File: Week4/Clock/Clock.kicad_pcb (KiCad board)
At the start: 2 copper layers, 140 x 90 mm, 48 parts, among them J1 Power_inlet_vertical, J2 Conn_01x06, SW1 RotaryEncoder_Switch, SW2 Omron_B3F_SPST, U2 ATmega328-PU, U3 L7805_TO92, U4 DS1307_DIP-8, U5 MAX7219, U6 MAX7219, Y1 Crystal 16MHZ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

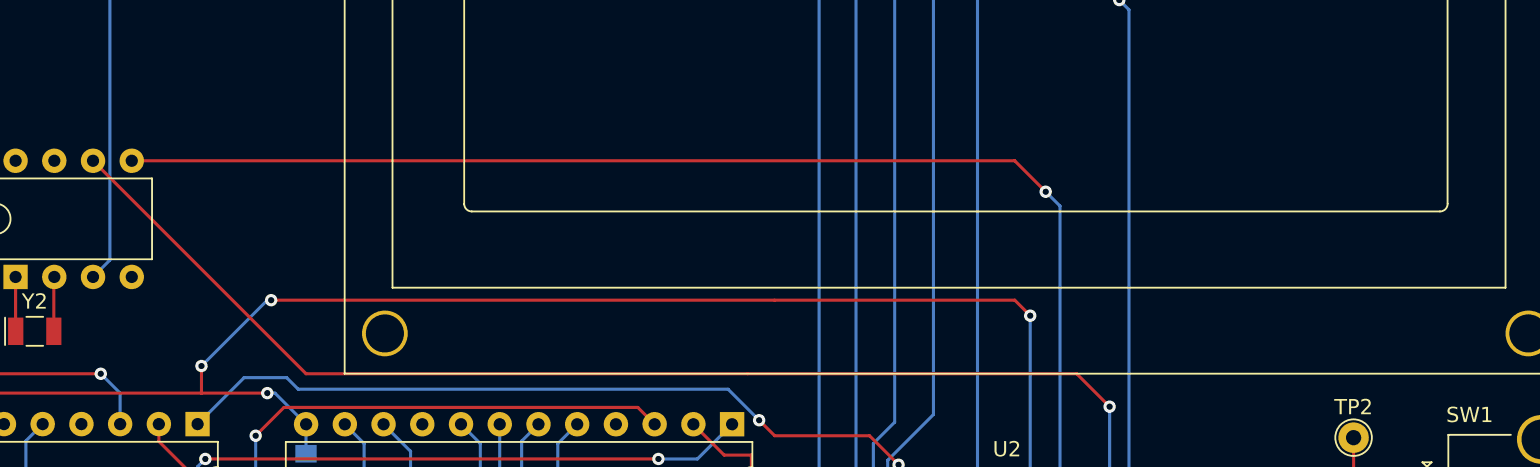
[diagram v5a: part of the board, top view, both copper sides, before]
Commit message: Week 6 Update* (Arduino Code)
Added additional Display modes now including Decimal and Binary mode found at https://bryang229.github.io/8x8Demo/ :) now we have 3 different ways to read time !
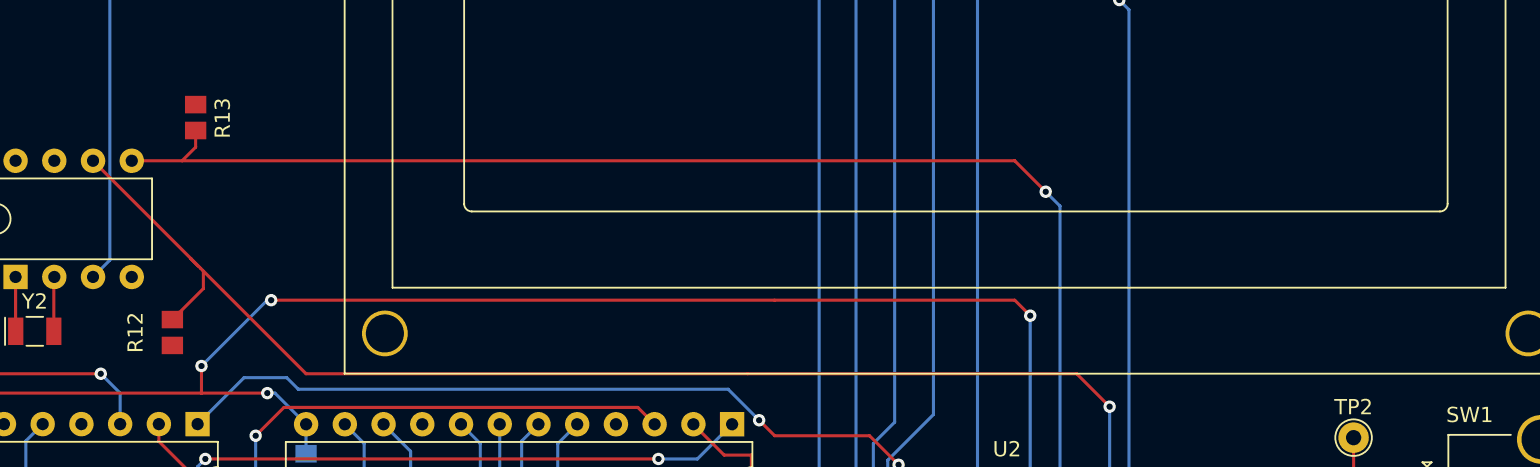
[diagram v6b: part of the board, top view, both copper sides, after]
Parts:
- added R12: R_0805_2.2K, footprints:R_0805_2012Metric, F.Cu at (118.7, 91.8)
- added R13: R_0805_2.2K, footprints:R_0805_2012Metric, F.Cu at (120.3, 77.7)
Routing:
- net A5 SCK: track 80.3 -> 85.1 mm
- net A4 SDA: track 84.0 -> 86.3 mm
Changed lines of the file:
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@@
     )
   )
+  (footprint "footprints:R_0805_2012Metric" (layer "F.Cu")
+    (at 118.745 91.782 90)
+    (descr "Resistor SMD 0805 (2012 Metric), square (rectangular) end terminal, IPC_7351 nominal, (Body size source: http://www.tortai-tech.com/upload/download/2011102023233369053.pdf), generated with kicad-footprint-generator")
+    (tags "resistor")
+    (property "Digikey PN" "311-2.20KCRCT-ND")
+    (property "MFG" "N/A")
+    (property "MPN" "N/A")
+    (property "Mouser PN" "N/A")
+    (property "Power" "N/A")
+    (property "Sheetfile" "Clock.kicad_sch")
+    (property "Sheetname" "")
+    (property "Tolerance" "N/A")
+    (attr smd)
+    (fp_text reference "R12" (at 0 -2.413 90) (layer "F.SilkS")
+      (effects (font (size 1 1) (thickness 0.15)))
+    )
+    (fp_text value "R_0805_2.2K" (at 0 1.65 90) (layer "F.Fab")
+      (effects (font (size 1 1) (thickness 0.15)))
+    )
+    (fp_text user "${REFERENCE}" (at 0 0 90) (layer "F.Fab")
+      (effects (font (size 0.5 0.5) (thickness 0.08)))
+    )
+    (fp_line (start -1.68 -0.95) (end 1.68 -0.95) (layer "F.CrtYd") (width 0.05))
+    (fp_line (start 1.68 0.95) (end -1.68 0.95) (layer "F.CrtYd") (width 0.05))
+    (fp_line (start -1.68 0.95) (end -1.68 -0.95) (layer "F.CrtYd") (width 0.05))
+    (fp_line (start 1.68 -0.95) (end 1.68 0.95) (layer "F.CrtYd") (width 0.05))
+    (fp_line (start -1 -0.6) (end 1 -0.6) (layer "F.Fab") (width 0.1))
+    (fp_line (start 1 -0.6) (end 1 0.6) (layer "F.Fab") (width 0.1))
+    (fp_line (start -1 0.6) (end -1 -0.6) (layer "F.Fab") (width 0.1))
+    (fp_line (start 1 0.6) (end -1 0.6) (layer "F.Fab") (width 0.1))
+    (pad "1" smd rect locked (at -0.85 0 90) (size 1.15 1.4) (layers "F.Cu" "F.Paste" "F.Mask")
+      (net 8 "VCC") (pintype "passive"))
+    (pad "2" smd rect locked (at 0.85 0 90) (size 1.15 1.4) (layers "F.Cu" "F.Paste" "F.Mask")
+      (net 39 "A5 SCK") (pintype "passive"))
+    (model "${HPS3DMOD}/R_0805_2012Metric.wrl"
+      (offset (xyz 0 0 0))
+      (scale (xyz 1 1 1))
+      (rotate (xyz 0 0 0))
+    )
+  )
   (footprint "footprints:Crystal_SMD_HC49-SD" (layer "F.Cu")
     (at 161.798 124.46 -90)
@@
       (net 43 "ROT ENC B OUT") (pinfunction "1") (pintype "passive"))
   )
+  (footprint "footprints:R_0805_2012Metric" (layer "F.Cu")
+    (at 120.269 77.685 -90)
+    (descr "Resistor SMD 0805 (2012 Metric), square (rectangular) end terminal, IPC_7351 nominal, (Body size source: http://www.tortai-tech.com/upload/download/2011102023233369053.pdf), generated with kicad-footprint-generator")
+    (tags "resistor")
+    (property "Digikey PN" "311-2.20KCRCT-ND")
+    (property "MFG" "N/A")
+    (property "MPN" "N/A")
+    (property "Mouser PN" "N/A")
+    (property "Power" "N/A")
+    (property "Sheetfile" "Clock.kicad_sch")
+    (property "Sheetname" "")
+    (property "Tolerance" "N/A")
+    (attr smd)
+    (fp_text reference "R13" (at 0.039 -1.778 90) (layer "F.SilkS")
+      (effects (font (size 1 1) (thickness 0.15)))
+    )
+    (fp_text value "R_0805_2.2K" (at 0 1.65 90) (layer "F.Fab")
+      (effects (font (size 1 1) (thickness 0.15)))
+    )
+    (fp_text user "${REFERENCE}" (at 0 0 90) (layer "F.Fab")
+      (effects (font (size 0.5 0.5) (thickness 0.08)))
+    )
+    (fp_line (start 1.68 -0.95) (end 1.68 0.95) (layer "F.CrtYd") (width 0.05))
+    (fp_line (start -1.68 -0.95) (end 1.68 -0.95) (layer "F.CrtYd") (width 0.05))
+    (fp_line (start 1.68 0.95) (end -1.68 0.95) (layer "F.CrtYd") (width 0.05))
+    (fp_line (start -1.68 0.95) (end -1.68 -0.95) (layer "F.CrtYd") (width 0.05))
+    (fp_line (start 1 0.6) (end -1 0.6) (layer "F.Fab") (width 0.1))
+    (fp_line (start 1 -0.6) (end 1 0.6) (layer "F.Fab") (width 0.1))
+    (fp_line (start -1 -0.6) (end 1 -0.6) (layer "F.Fab") (width 0.1))
+    (fp_line (start -1 0.6) (end -1 -0.6) (layer "F.Fab") (width 0.1))
+    (pad "1" smd rect locked (at -0.85 0 270) (size 1.15 1.4) (layers "F.Cu" "F.Paste" "F.Mask")
+      (net 8 "VCC") (pintype "passive"))
+    (pad "2" smd rect locked (at 0.85 0 270) (size 1.15 1.4) (layers "F.Cu" "F.Paste" "F.Mask")
+      (net 37 "A4 SDA") (pintype "passive"))
+    (model "${HPS3DMOD}/R_0805_2012Metric.wrl"
+      (offset (xyz 0 0 0))
+      (scale (xyz 1 1 1))
+      (rotate (xyz 0 0 0))
+    )
+  )
   (footprint "footprints:MountingHole_3.2mm_M3" locked (layer "F.Cu")
     (at 85 60)
@@
     (fp_arc (start 63.7 8) (mid 64.053553 8.146447) (end 64.2 8.5) (layer "F.SilkS") (width 0.12))
     (fp_arc (start 0.20066 22.9997) (mid -0.153162 22.853142) (end -0.29972 22.49932) (layer "F.SilkS") (width 0.12))
-    (fp_arc (start 64.20104 22.49932) (mid 64.054473 22.853115) (end 63.70066 22.9997) (layer "F.SilkS") (width 0.12))
+    (fp_arc (start 64.20104 22.49932) (mid 64.054479 22.85315) (end 63.70066 22.9997) (layer "F.SilkS") (width 0.12))
     (fp_line (start -8.25 -2.75) (end 72.25 -2.75) (layer "F.CrtYd") (width 0.05))
     (fp_line (start -8.25 33.75) (end 72.25 33.75) (layer "F.CrtYd") (width 0.05))
@@
   (segment (start 104.14 115.316) (end 102.616 113.792) (width 0.2032) (layer "B.Cu") (net 35))
   (segment (start 108.458 88.138) (end 108.458 91.694) (width 0.2032) (layer "F.Cu") (net 36))
-  (segment (start 173.99 80.518) (end 116.078 80.518) (width 0.2032) (layer "F.Cu") (net 37))
+  (segment (start 119.38 80.518) (end 116.078 80.518) (width 0.2032) (layer "F.Cu") (net 37))
+  (segment (start 173.99 80.518) (end 119.38 80.518) (width 0.2032) (layer "F.Cu") (net 37))
+  (segment (start 120.269 79.629) (end 119.38 80.518) (width 0.2032) (layer "F.Cu") (net 37))
+  (segment (start 120.269 78.535) (end 120.269 79.629) (width 0.2032) (layer "F.Cu") (net 37))
   (segment (start 176.022 82.55) (end 173.99 80.518) (width 0.2032) (layer "F.Cu") (net 37))
   (via (at 176.022 82.55) (size 0.8128) (drill 0.4064) (layers "F.Cu" "B.Cu") (net 37))
@@
   (segment (start 176.959689 83.487689) (end 176.959689 103.807689) (width 0.2032) (layer "B.Cu") (net 37))
   (segment (start 110.968 91.704) (end 110.968 88.168) (width 0.2032) (layer "F.Cu") (net 38))
-  (segment (start 127.508 94.488) (end 113.538 80.518) (width 0.2032) (layer "F.Cu") (net 39))
+  (segment (start 118.745 90.932) (end 120.777 88.9) (width 0.2032) (layer "F.Cu") (net 39))
   (segment (start 156.464 94.488) (end 178.054 94.488) (width 0.2032) (layer "F.Cu") (net 39))
+  (segment (start 120.777 87.757) (end 120.5865 87.5665) (width 0.2032) (layer "F.Cu") (net 39))
+  (segment (start 120.5865 87.5665) (end 119.9515 86.9315) (width 0.2032) (layer "F.Cu") (net 39))
+  (segment (start 120.777 88.9) (end 120.777 87.757) (width 0.2032) (layer "F.Cu") (net 39))
+  (segment (start 120.4595 87.4395) (end 119.9515 86.9315) (width 0.2032) (layer "F.Cu") (net 39))
+  (segment (start 127.508 94.488) (end 120.777 87.757) (width 0.2032) (layer "F.Cu") (net 39))
   (segment (start 178.054 94.488) (end 180.213 96.647) (width 0.2032) (layer "F.Cu") (net 39))
   (segment (start 156.464 94.488) (end 127.508 94.488) (width 0.2032) (layer "F.Cu") (net 39))
+  (segment (start 119.9515 86.9315) (end 113.538 80.518) (width 0.2032) (layer "F.Cu") (net 39))
   (via (at 180.213 96.647) (size 0.8128) (drill 0.4064) (layers "F.Cu" "B.Cu") (net 39))
   (segment (start 178.679 102.372) (end 178.064 102.372) (width 0.2032) (layer "B.Cu") (net 39))

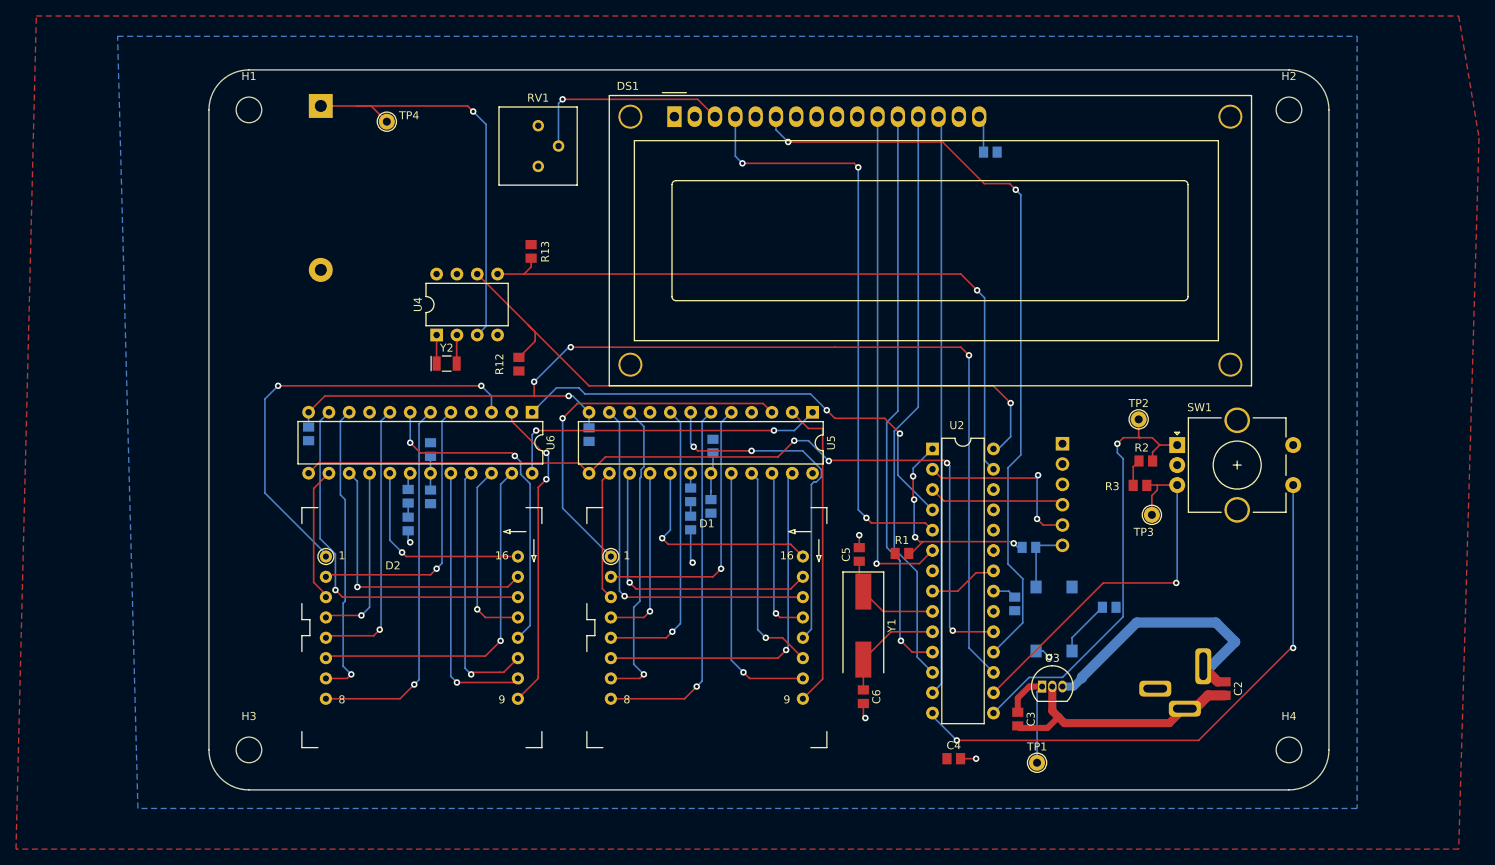
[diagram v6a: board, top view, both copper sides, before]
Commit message: Added Rounded Tracing (Passing all DRC)
It's so perty (pretty :))
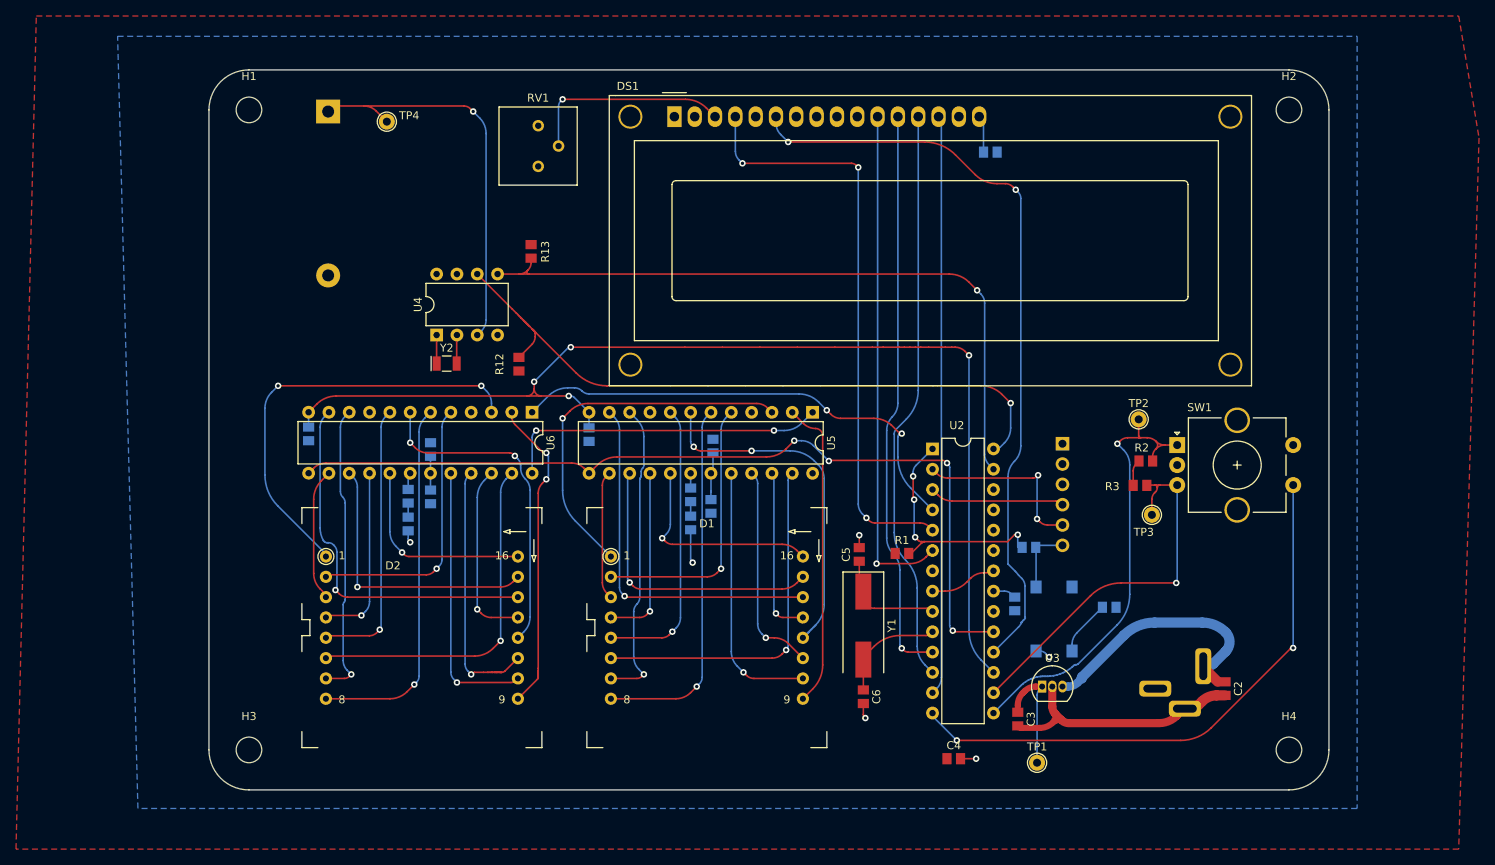
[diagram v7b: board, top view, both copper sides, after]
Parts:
- moved BT1 1.15 mm to (94.9, 60.2)
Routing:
- net VBAT: track 53.0 -> 51.1 mm
- net ~{RST}: track 28.4 -> 30.3 mm
- net ROT ENC A OUT: track 56.0 -> 57.5 mm
- net Net-(C2-Pad1): track 34.9 -> 33.5 mm
- net A5 SCK: track 85.1 -> 83.7 mm
- net DATA MAX: track 139.8 -> 141.1 mm
- net SCK: track 110.2 -> 109.0 mm
- net LCD D6: track 72.7 -> 71.8 mm
- net LCD E: track 95.7 -> 94.9 mm
- net A4 SDA: track 86.3 -> 87.1 mm
- net Net-(D1-Pad9): track 39.5 -> 38.7 mm
- net LOAD MAX: track 61.0 -> 60.5 mm
- net Net-(D2-Pad12): track 41.7 -> 41.2 mm
- net Net-(C5-Pad1): track 13.7 -> 14.2 mm
- net Net-(D1-Pad1): track 47.2 -> 46.7 mm
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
